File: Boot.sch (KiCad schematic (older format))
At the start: 6 parts, among them SW1 SW_PUSH, U2 SN74LVC1G373

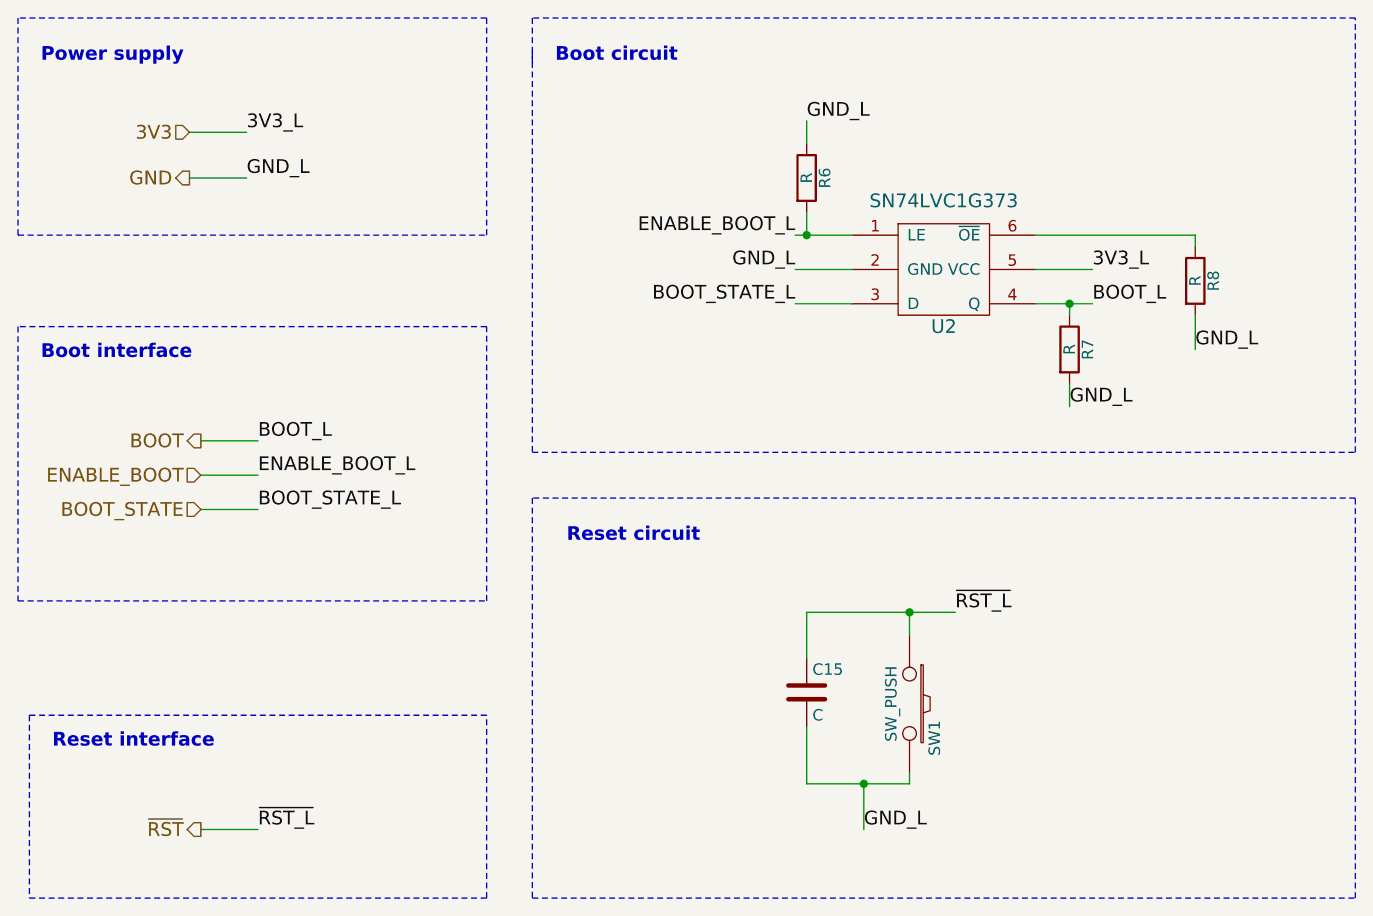
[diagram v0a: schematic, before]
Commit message: - #4 Added UART and CAN interface transceivers - Improved schematic structure - Removed all gerber outputs - Generated schematics outputs for PCB design - Updated local libraries
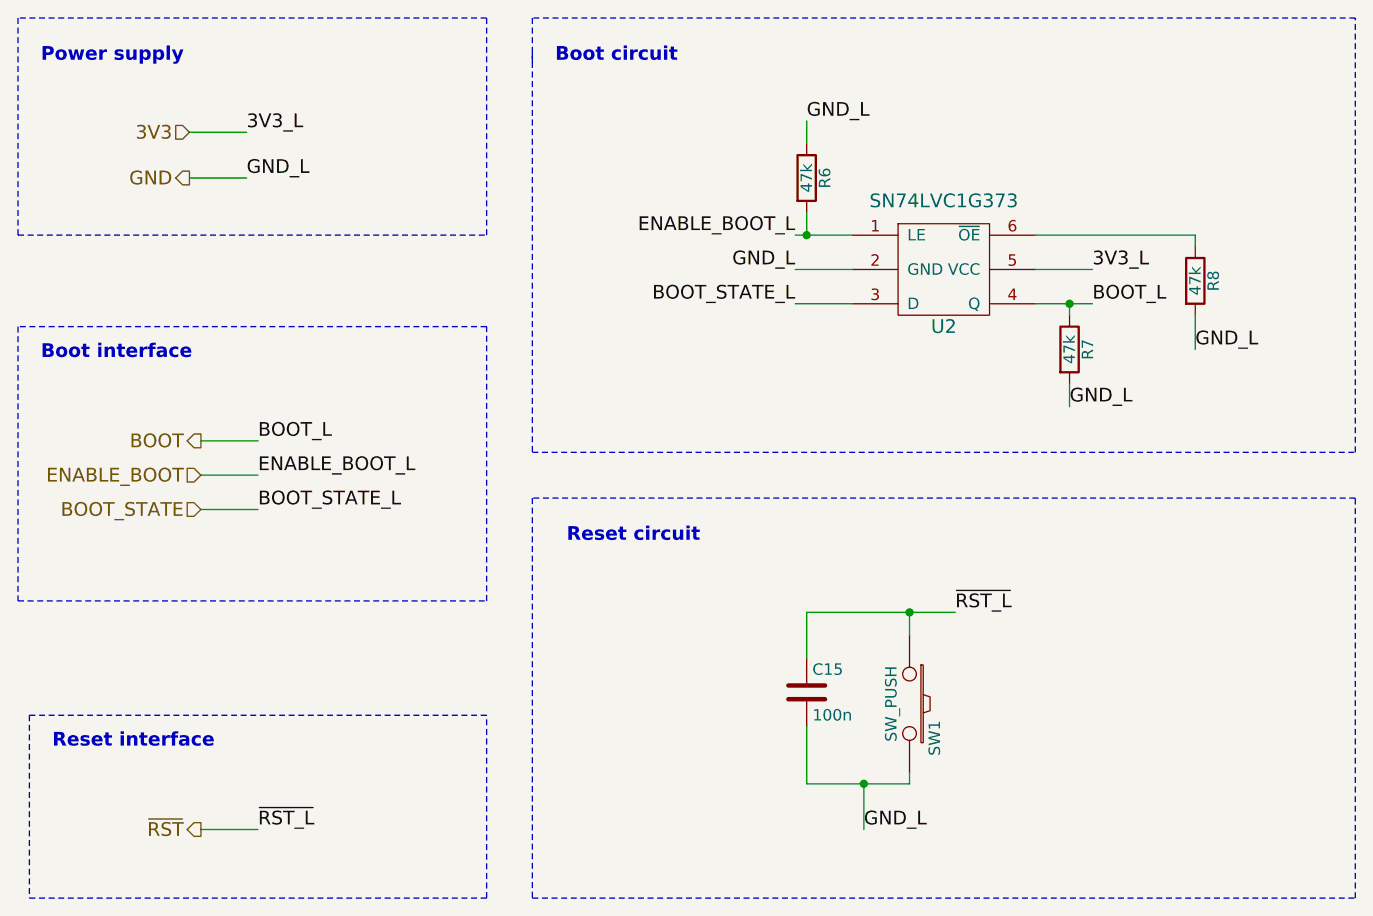
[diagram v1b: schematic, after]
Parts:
- C15: value C -> 100n; footprint (none) -> Capacitors_SMD:C_0603_HandSoldering
- R6, R7, R8: value R -> 47k; footprint (none) -> Resistors_SMD:R_0603_HandSoldering
- SW1: footprint (none) -> ComponentLib:SW_PUSH_SMALL_SMD
- U2: footprint (none) -> TO_SOT_Packages_SMD:SOT-23-6
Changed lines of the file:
@@
 P 6750 4950
 F 0 "C15" H 6775 5050 50  0000 L CNN
-F 1 "C" H 6775 4850 50  0000 L CNN
-F 2 "" H 6788 4800 30  0000 C CNN
+F 1 "100n" H 6775 4850 50  0000 L CNN
+F 2 "Capacitors_SMD:C_0603_HandSoldering" H 6788 4800 30  0001 C CNN
 F 3 "" H 6750 4950 60  0000 C CNN
 	1    6750 4950
@@
 F 0 "SW1" H 7350 5110 50  0000 C CNN
 F 1 "SW_PUSH" H 7200 4920 50  0000 C CNN
-F 2 "" H 7200 5000 60  0000 C CNN
+F 2 "ComponentLib:SW_PUSH_SMALL_SMD" H 7200 5000 60  0001 C CNN
 F 3 "" H 7200 5000 60  0000 C CNN
 	1    7200 5000
@@
 F 0 "U2" H 7350 2850 60  0000 C CNN
 F 1 "SN74LVC1G373" H 7350 3400 60  0000 C CNN
-F 2 "" H 7350 3100 60  0000 C CNN
+F 2 "TO_SOT_Packages_SMD:SOT-23-6" H 7350 3100 60  0001 C CNN
 F 3 "" H 7350 3100 60  0000 C CNN
 	1    7350 3100
@@
 P 8450 3150
 F 0 "R8" V 8530 3150 50  0000 C CNN
-F 1 "R" V 8450 3150 50  0000 C CNN
-F 2 "" V 8380 3150 30  0000 C CNN
+F 1 "47k" V 8450 3150 50  0000 C CNN
+F 2 "Resistors_SMD:R_0603_HandSoldering" V 8380 3150 30  0001 C CNN
 F 3 "" H 8450 3150 30  0000 C CNN
 	1    8450 3150
@@
 P 7900 3450
 F 0 "R7" V 7980 3450 50  0000 C CNN
-F 1 "R" V 7900 3450 50  0000 C CNN
-F 2 "" V 7830 3450 30  0000 C CNN
+F 1 "47k" V 7900 3450 50  0000 C CNN
+F 2 "Resistors_SMD:R_0603_HandSoldering" V 7830 3450 30  0001 C CNN
 F 3 "" H 7900 3450 30  0000 C CNN
 	1    7900 3450
@@
 P 6750 2700
 F 0 "R6" V 6830 2700 50  0000 C CNN
-F 1 "R" V 6750 2700 50  0000 C CNN
-F 2 "" V 6680 2700 30  0000 C CNN
+F 1 "47k" V 6750 2700 50  0000 C CNN
+F 2 "Resistors_SMD:R_0603_HandSoldering" V 6680 2700 30  0001 C CNN
 F 3 "" H 6750 2700 30  0000 C CNN
 	1    6750 2700
